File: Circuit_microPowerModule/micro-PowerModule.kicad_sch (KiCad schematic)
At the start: 10 parts, among them J101 Screw_Terminal_01x02, J102 Jack-DC

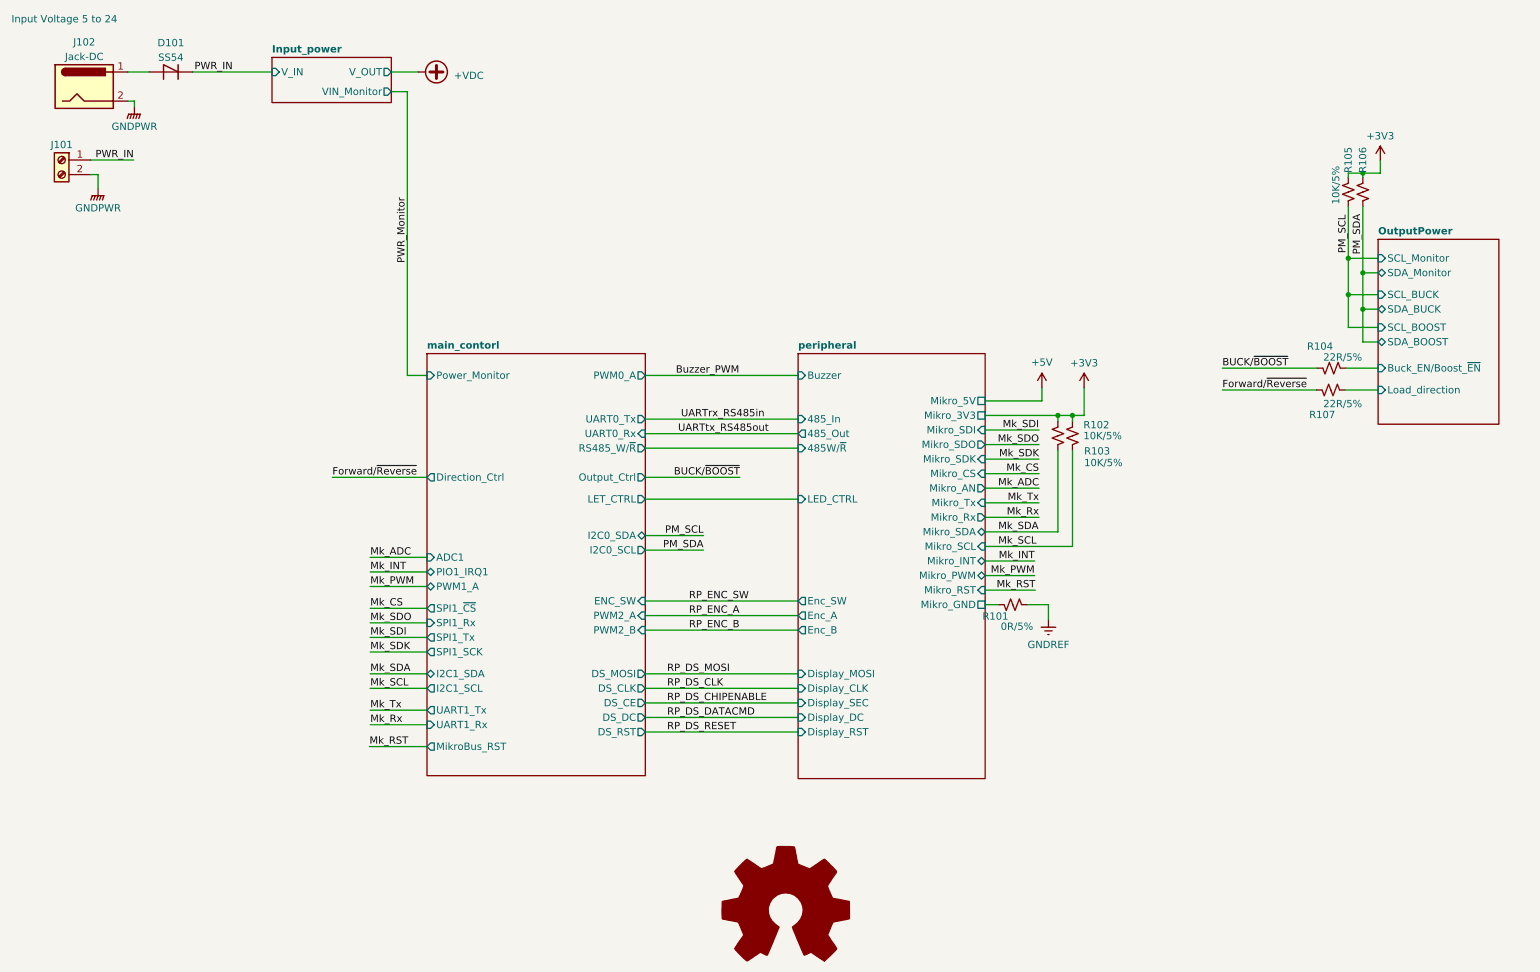
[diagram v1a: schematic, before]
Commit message: modify ERC warning
modify OPA, TVS-Diode, Cap
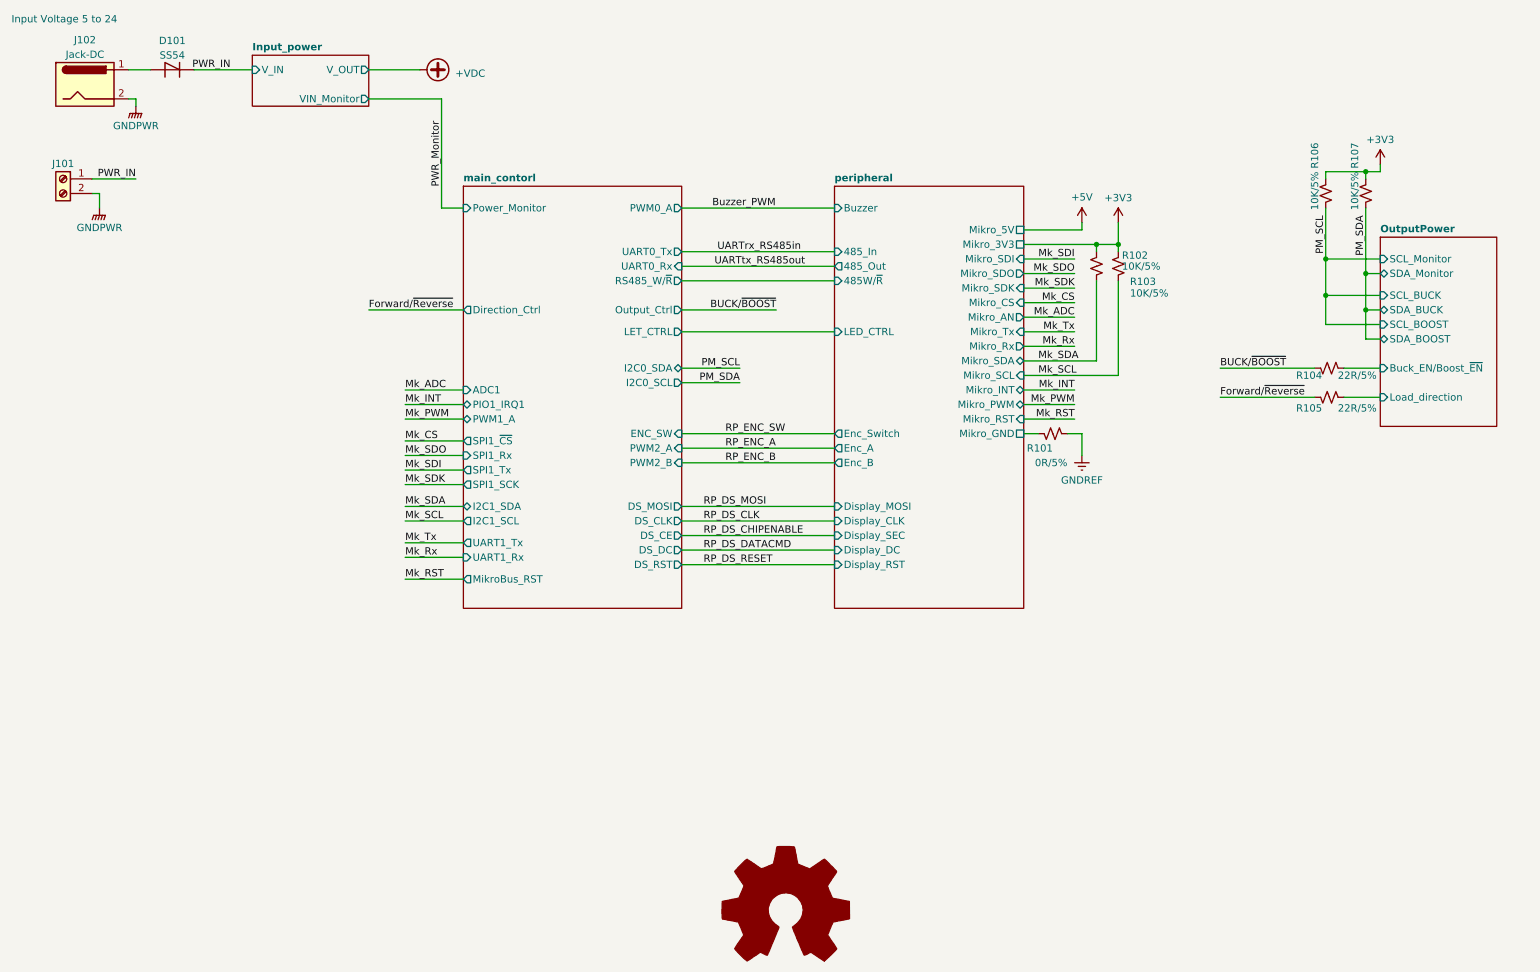
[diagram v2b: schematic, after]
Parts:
- renumbered R107 to R105, R105 to R106, R106 to R107
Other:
- sheet peripheral ports: added Enc_Switch; removed Enc_SW
- moved on the sheet: J101, R101, R102, R103, R105, R106, R107

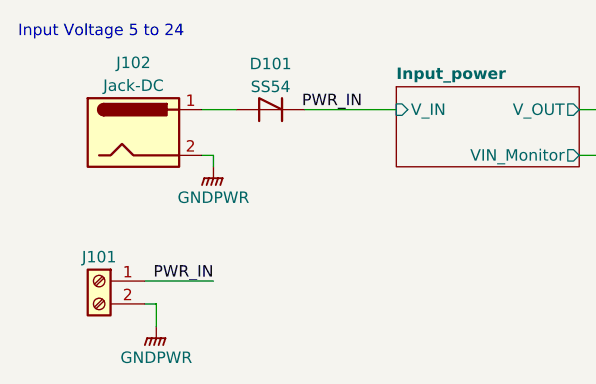
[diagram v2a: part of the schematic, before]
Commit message: start pcb layout
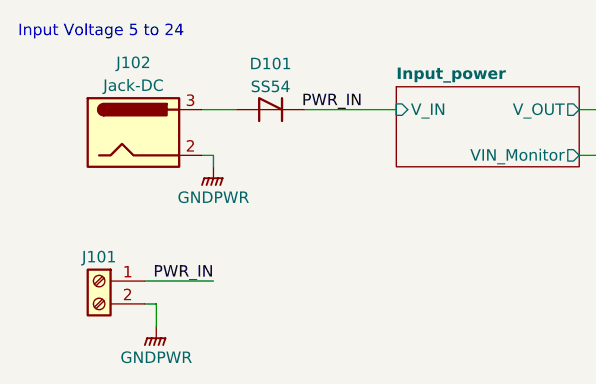
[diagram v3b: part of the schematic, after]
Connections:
- net GNDPWR: now also J102.1
- net at D101.2 (A): now also J102.3; no longer J102.1
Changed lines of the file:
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@@
       (effects (font (size 1.27 1.27)) hide)
     )
-    (property "Sim.Pins" "1=+ 2=-" (at 38.1 33.02 0)
+    (property "Sim.Pins" "1=+ 2=- 3=-" (at 38.1 33.02 0)
       (effects (font (size 1.27 1.27)) hide)
     )
@@
     )
     (pin "1")
+    (pin "3")
     (pin "2")
     (instances
